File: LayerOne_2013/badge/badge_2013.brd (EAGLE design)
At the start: 81.3 x 81.3 mm, 81 parts, among them CON6 J8, CON8 J3, J6 con1, U1 UG-2864HSWEG01, U3 TL064D

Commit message: usb
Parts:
- removed U$1: USB-MINIB-5PIN, SparkFun:USB-MINIB
- added JP6: USB-RECEPTABLE, daspilker:FCI-10103594-0001LF
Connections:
- net D+: now also JP6.3; no longer U$1.D+
- net D-: now also JP6.2; no longer U$1.D-
- net GND: now also JP6.5; no longer U$1.GND
- net VBUS: now also JP6.1; no longer U$1.VBUS
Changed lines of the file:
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@@
 <setting verticaltext="up"/>
 </settings>
-<grid distance="0.05" unitdist="inch" unit="inch" style="lines" multiple="1" display="yes" altdistance="0.005" altunitdist="inch" altunit="inch"/>
+<grid distance="0.05" unitdist="inch" unit="inch" style="lines" multiple="1" display="no" altdistance="0.005" altunitdist="inch" altunit="inch"/>
 <layers>
 <layer number="1" name="Top" color="4" fill="1" visible="yes" active="yes"/>
@@
 <element name="LED48" library="led" package="LED3MM" value="" x="4.97331875" y="37.77488125" rot="R172.5"/>
 <element name="U3" library="linear" package="SO14" value="TL064D" x="27.94" y="10.16"/>
-<element name="U$1" library="SparkFun" package="USB-MINIB" value="USB-MINIB-5PIN" x="-27.94" y="1.27" rot="MR180"/>
 <element name="BAT1" library="tvbgone-adj" package="BATTERY_CR123A" value="CR123A" x="0" y="0" rot="MR180"/>
 <element name="U1" library="microbuilder" package="UG-2864HSWEG01_0.96IN_WRAPAROUND" value="UG-2864HSWEG01" x="0" y="25.4" rot="MR180"/>
@@
 <element name="D3" library="microbuilder" package="CHIPLED_0805" value="" x="-17.78" y="-3.81"/>
 <element name="C12" library="SparkFun" package="0805" value="0.1uF" x="26.67" y="-17.78"/>
+<element name="JP6" library="daspilker" package="FCI-10103594-0001LF" value="USB-RECEPTABLE" x="-35.56" y="-46.99"/>
 </elements>
 <signals>
@@
 <contactref element="C21" pad="1"/>
 <contactref element="C19" pad="1"/>
-<contactref element="U$1" pad="GND"/>
 <contactref element="U1" pad="1"/>
 <contactref element="CON6" pad="1"/>
@@
 <contactref element="IC3" pad="1"/>
 <contactref element="BAT1" pad="-"/>
-<wire x1="26.4" y1="0.75" x2="22.86" y2="13.97" width="0" layer="19" extent="16-16"/>
-<wire x1="28.31" y1="-2.54" x2="26.4" y2="0.75" width="0" layer="19" extent="1-16"/>
+<contactref element="JP6" pad="5"/>
+<wire x1="-17.78" y1="-2.76" x2="-34.26" y2="-42.465" width="0" layer="19" extent="1-1"/>
+<wire x1="-19" y1="0" x2="-17.78" y2="-2.76" width="0" layer="19" extent="1-1"/>
+<wire x1="-12.7" y1="-2.76" x2="-17.78" y2="-2.76" width="0" layer="19" extent="1-1"/>
+<wire x1="-23.065" y1="3.95" x2="-19" y2="0" width="0" layer="19" extent="1-1"/>
+<wire x1="-5.75" y1="-1.6" x2="-12.7" y2="-2.76" width="0" layer="19" extent="1-1"/>
+<wire x1="0.8" y1="-5.75" x2="-5.75" y2="-1.6" width="0" layer="19" extent="1-1"/>
+<wire x1="5.75" y1="1.6" x2="0.8" y2="-5.75" width="0" layer="19" extent="1-1"/>
+<wire x1="0.8" y1="5.75" x2="5.75" y2="1.6" width="0" layer="19" extent="1-1"/>
+<wire x1="23.065" y1="-3.95" x2="5.75" y2="1.6" width="0" layer="19" extent="1-1"/>
+<wire x1="24.5" y1="-2.54" x2="23.065" y2="-3.95" width="0" layer="19" extent="1-1"/>
+<wire x1="28.31" y1="-2.54" x2="24.5" y2="-2.54" width="0" layer="19" extent="1-1"/>
 <wire x1="32.12" y1="-2.54" x2="28.31" y2="-2.54" width="0" layer="19" extent="1-1"/>
-<wire x1="24.5" y1="-2.54" x2="26.4" y2="0.75" width="0" layer="19" extent="1-16"/>
-<wire x1="23.065" y1="-3.95" x2="24.5" y2="-2.54" width="0" layer="19" extent="1-1"/>
+<wire x1="26.4" y1="0.75" x2="24.5" y2="-2.54" width="0" layer="19" extent="1-16"/>
 <wire x1="25.72" y1="-10.16" x2="23.065" y2="-3.95" width="0" layer="19" extent="1-1"/>
 <wire x1="30.8" y1="-10.16" x2="25.72" y2="-10.16" width="0" layer="19" extent="1-1"/>
 <wire x1="27.57" y1="-17.78" x2="25.72" y2="-10.16" width="0" layer="19" extent="1-1"/>
-<wire x1="5.75" y1="1.6" x2="23.065" y2="-3.95" width="0" layer="19" extent="1-1"/>
-<wire x1="0.8" y1="5.75" x2="5.75" y2="1.6" width="0" layer="19" extent="1-1"/>
-<wire x1="0.8" y1="-5.75" x2="5.75" y2="1.6" width="0" layer="19" extent="1-1"/>
-<wire x1="-5.75" y1="-1.6" x2="0.8" y2="-5.75" width="0" layer="19" extent="1-1"/>
-<wire x1="-12.7" y1="-2.76" x2="-5.75" y2="-1.6" width="0" layer="19" extent="1-1"/>
-<wire x1="-17.78" y1="-2.76" x2="-12.7" y2="-2.76" width="0" layer="19" extent="1-1"/>
-<wire x1="-19" y1="0" x2="-17.78" y2="-2.76" width="0" layer="19" extent="1-1"/>
-<wire x1="-23.065" y1="3.95" x2="-19" y2="0" width="0" layer="19" extent="1-1"/>
-<wire x1="-25.44" y1="2.87" x2="-23.065" y2="3.95" width="0" layer="19" extent="1-16"/>
-<wire x1="-10.15" y1="26.6" x2="0.8" y2="5.75" width="0" layer="19" extent="1-16"/>
+<wire x1="22.86" y1="13.97" x2="26.4" y2="0.75" width="0" layer="19" extent="16-16"/>
+<wire x1="-10.15" y1="26.6" x2="0.8" y2="5.75" width="0" layer="19" extent="1-1"/>
 </signal>
 <signal name="N$2">
@@
 </signal>
 <signal name="VBUS">
-<contactref element="U$1" pad="VBUS"/>
 <contactref element="D1" pad="4"/>
-<wire x1="24.4" y1="0.95" x2="-25.44" y2="-0.33" width="0" layer="19" extent="16-16"/>
+<contactref element="JP6" pad="1"/>
+<wire x1="24.4" y1="0.95" x2="-36.86" y2="-42.465" width="0" layer="19" extent="1-16"/>
 </signal>
 <signal name="D-">
 <contactref element="D1" pad="2"/>
-<contactref element="U$1" pad="D-"/>
-<wire x1="-25.44" y1="0.47" x2="26.4" y2="-0.95" width="0" layer="19" extent="16-16"/>
+<contactref element="JP6" pad="2"/>
+<wire x1="26.4" y1="-0.95" x2="-36.21" y2="-42.465" width="0" layer="19" extent="1-16"/>
 </signal>
 <signal name="D+">
 <contactref element="D1" pad="3"/>
-<contactref element="U$1" pad="D+"/>
-<wire x1="24.4" y1="-0.95" x2="-25.44" y2="1.27" width="0" layer="19" extent="16-16"/>
+<contactref element="JP6" pad="3"/>
+<wire x1="24.4" y1="-0.95" x2="-35.56" y2="-42.465" width="0" layer="19" extent="1-16"/>
 </signal>
 <signal name="N$21">

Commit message: 
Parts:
- renumbered R1 to R1T, R2 to R2T
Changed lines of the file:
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@@
 <element name="IC2" library="Outline" package="NONOLITH_TQFP-44" value="" x="0" y="0"/>
 <element name="IC1" library="23b_clock_noleds" package="HTSSOP32DAP" value="" x="-27.94" y="0" rot="R180"/>
-<element name="R1" library="rcl" package="R0805" value="20K" x="31.75" y="-10.16"/>
+<element name="R1T" library="rcl" package="R0805" value="20K" x="31.75" y="-10.16"/>
 <element name="IC3" library="23b_clock_noleds" package="HTSSOP32DAP" value="" x="27.94" y="0"/>
-<element name="R2" library="rcl" package="R0805" value="20K" x="26.67" y="-10.16"/>
+<element name="R2T" library="rcl" package="R0805" value="20K" x="26.67" y="-10.16"/>
 <element name="LED1" library="led" package="LED3MM" value="" x="0" y="38.1" rot="R180"/>
 <element name="LED2" library="led" package="LED3MM" value="" x="-4.97331875" y="37.77488125" rot="R187.5"/>
@@
 <contactref element="D3" pad="C"/>
 <contactref element="C12" pad="2"/>
-<contactref element="R1" pad="1"/>
+<contactref element="R1T" pad="1"/>
 <contactref element="IC1" pad="1"/>
-<contactref element="R2" pad="1"/>
+<contactref element="R2T" pad="1"/>
 <contactref element="IC3" pad="1"/>
 <contactref element="BAT1" pad="-"/>
@@
 <signal name="N$13">
 <contactref element="IC1" pad="31"/>
-<contactref element="R1" pad="2"/>
+<contactref element="R1T" pad="2"/>
 <wire x1="32.7" y1="-10.16" x2="-23.715" y2="-3.95" width="0" layer="19" extent="1-1"/>
 </signal>
@@
 <signal name="N$1">
 <contactref element="IC3" pad="31"/>
-<contactref element="R2" pad="2"/>
+<contactref element="R2T" pad="2"/>
 <wire x1="27.62" y1="-10.16" x2="23.715" y2="3.95" width="0" layer="19" extent="1-1"/>
 </signal>

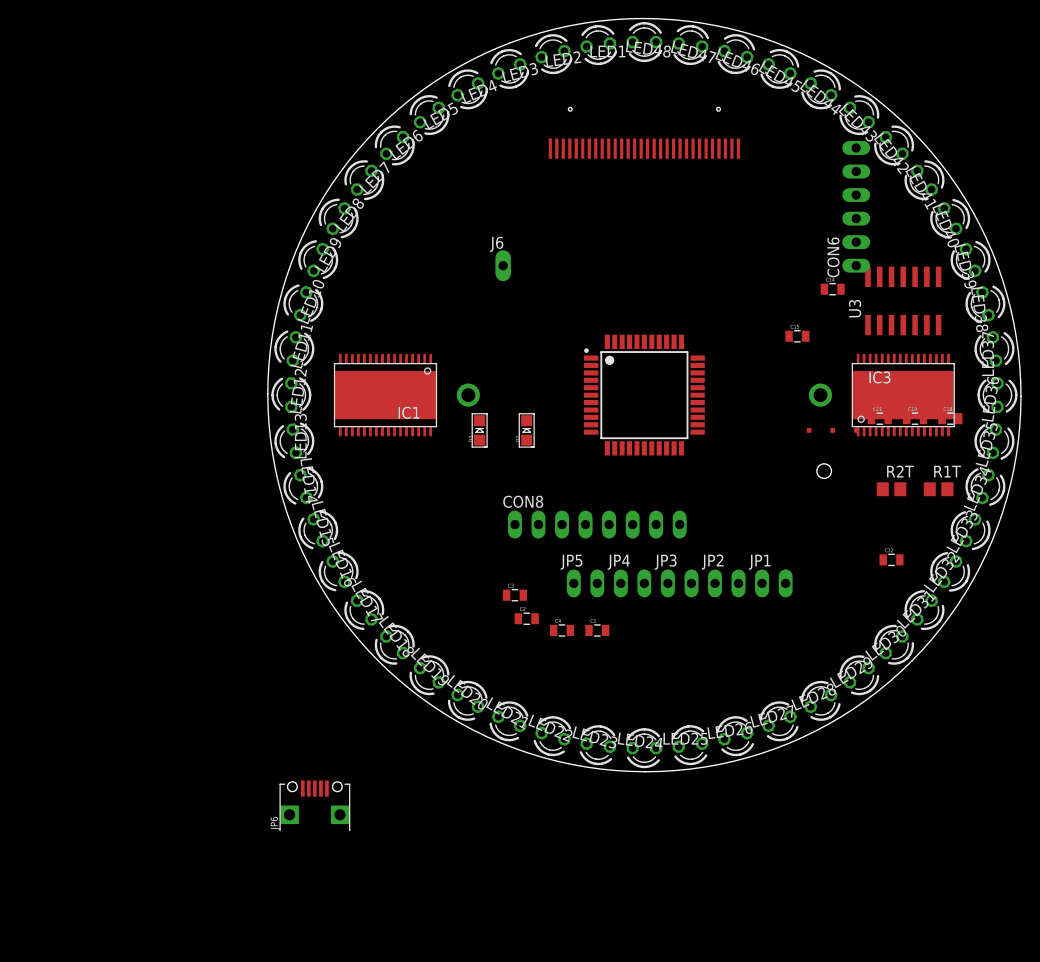
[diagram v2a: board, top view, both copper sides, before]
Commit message: 
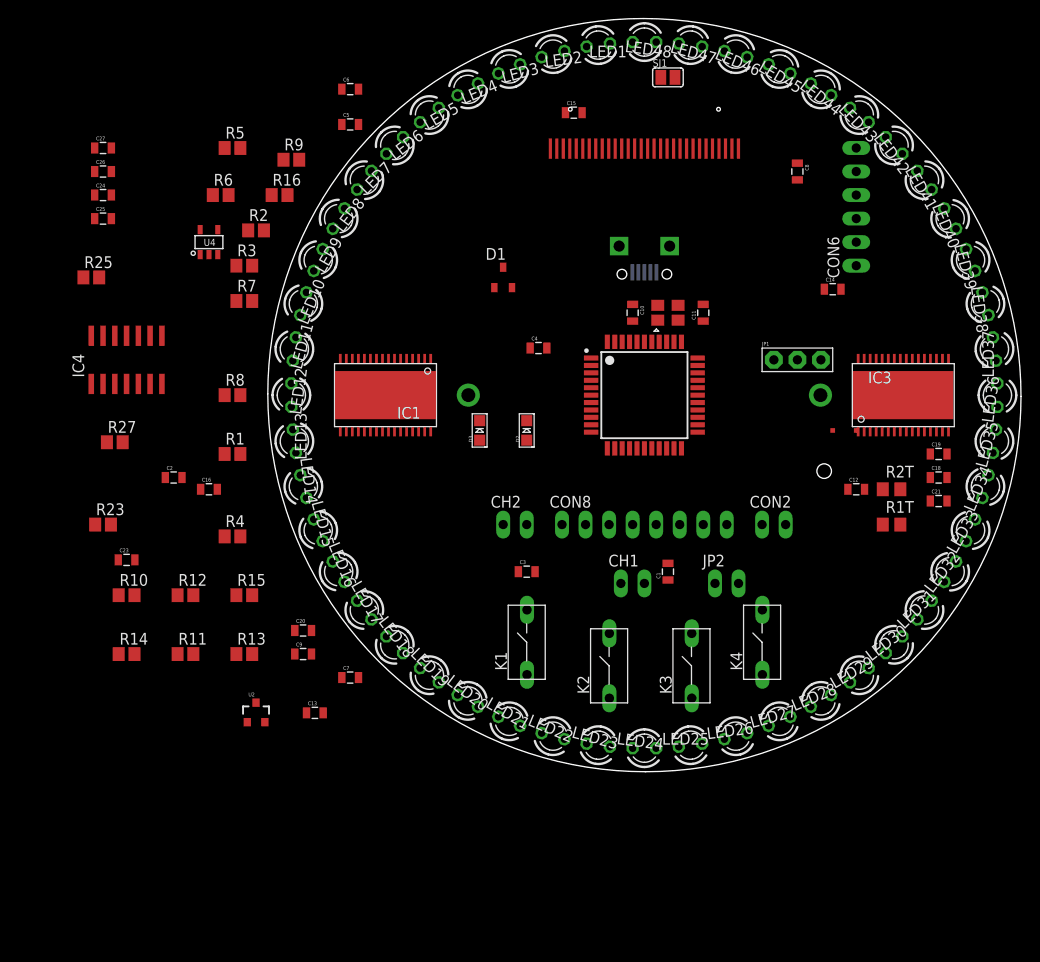
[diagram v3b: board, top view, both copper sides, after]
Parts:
- removed J6: con1, microbuilder:1X01_OVAL
- removed JP3, JP5: (no value), microbuilder:1X02_OVAL
- removed TP3: TEST-POINT2, SparkFun:PAD.02X.02
- removed U3: TL064D, linear:SO14
- added C10, C11, C24, C26, C5, C6, C7: 0.1uF, SparkFun:0805
- added C13, C20, C27, C8: 4.7uF, SparkFun:0805
- added C16, C9: 330pF, SparkFun:0805
- added C23: 10pF, SparkFun:0805
- added C25: 1uF, SparkFun:0805
- added CH2: CON2, microbuilder:1X02_OVAL
- added CON2: EXT, microbuilder:1X02_OVAL
- added IC4: TL064D, linear:SO14
- added K1, K2, K3, K4: (no value), switch-omron:B3F-5XX
- added R1, R11, R13, R4, R5, R6: 3K, resistor:R0805
- added R10, R2: 820K, resistor:R0805
- added R12, R27, R3: 180K, resistor:R0805
- added R14, R7: 20K, resistor:R0805
- added R15, R8: 180k, resistor:R0805
- added R16: 820k, resistor:R0805
- added R23, R25: 360K, resistor:R0805
- added R9: 20.0K, resistor:R0805
- added SJ1: (no value), microbuilder:SOLDERJUMPER_REFLOW_NOPASTE
- added U2: AP7333-33SOT23-3, SparkFun:SOT23-3
- added U4: TPS60403, RHD2000_eval_board:SOT-23-5
- added X2: NX3225GA, M6-RF315:NX3225GA
- added Z1: PRTR5V0U2X, USBug:SOT143B
- C1: value 0.1uF -> 1uF
- C2: value 0.1uF -> 330pF
- CH1: value (none) -> CON2
- D1: value PRTR5V0U2X -> LM4040d20; device USBug:SOT143B -> texas:DBZ_R-PDSO-G3
- JP1: device microbuilder:1X02_OVAL -> microbuilder:JUMPER3
- TP1: value TEST-POINT2 -> TP-2.048V
- TP2: value TEST-POINT2 -> (none)
- moved JP6 73.9 mm to (0.00, 17.8), flipped to the bottom, turned to 180 degrees
- moved D1 42.6 mm to (-15.2, 12.7), flipped to the top, turned to 0 degrees
- moved C2 41.0 mm to (-50.8, -8.89)
- moved C15 34.1 mm to (-7.62, 30.5)
- moved C4 30.6 mm to (-11.4, 5.08)
- moved JP1 24.3 mm to (16.5, 3.81)
- moved C21 10.9 mm to (31.8, -11.4)
- moved C1 9.92 mm to (2.54, -19.1), turned to 90 degrees
- moved C12 8.52 mm to (22.9, -10.2)
- moved C18 6.48 mm to (31.8, -8.89)
- moved R1T 6.35 mm to (26.7, -14.0)
- moved CON8 5.08 mm to (0.00, -14.0)
- moved C19 4.58 mm to (31.8, -6.35)
- moved C3 2.84 mm to (-12.7, -19.1)
- renumbered JP4 to CH1
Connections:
- net N$6 renamed RX
- net N$7 renamed PWR
- net N$8 renamed TX
- net N$9 renamed LNK
- removed net V+: U3.4
- removed net V-: U3.11
- removed net VBAT: U1.6
- removed net VCC: BAT1.+, C18.2, C19.2, C21.2, IC1.32, IC2.19, IC2.31, IC2.9, IC3.32, LED1.A, LED10.A, LED11.A, LED12.A, LED13.A, LED14.A, LED15.A, LED16.A, LED17.A, LED18.A, LED19.A, LED2.A, LED20.A, LED21.A, LED22.A, LED23.A, LED24.A, LED25.A, LED26.A, LED27.A, LED28.A, LED29.A, LED3.A, LED30.A, LED31.A, LED32.A, LED33.A, LED34.A, LED35.A, LED36.A, LED37.A, LED38.A, LED39.A, LED4.A, LED40.A, LED41.A, LED42.A, LED43.A, LED44.A, LED45.A, LED46.A, LED47.A, LED48.A, LED5.A, LED6.A, LED7.A, LED8.A, LED9.A, U1.28
- removed net VDD: U1.9
- removed net VLSS: U1.29
- removed net VSS: U1.8
- new net !CS: IC2.4, U1.13
- new net !RES: IC2.5, U1.14
- new net +2.048V: C5.1, IC2.40, IC4.8, IC4.9, R13.1, R25.1, R4.1, R6.1, TP1.P$1
- new net +3.3V: C18.2, C19.2, C20.1, C21.2, IC1.32, IC2.19, IC2.31, IC2.9, IC3.32, JP1.2, LED1.A, LED10.A, LED11.A, LED12.A, LED13.A, LED14.A, LED15.A, LED16.A, LED17.A, LED18.A, LED19.A, LED2.A, LED20.A, LED21.A, LED22.A, LED23.A, LED24.A, LED25.A, LED26.A, LED27.A, LED28.A, LED29.A, LED3.A, LED30.A, LED31.A, LED32.A, LED33.A, LED34.A, LED35.A, LED36.A, LED37.A, LED38.A, LED39.A, LED4.A, LED40.A, LED41.A, LED42.A, LED43.A, LED44.A, LED45.A, LED46.A, LED47.A, LED48.A, LED5.A, LED6.A, LED7.A, LED8.A, LED9.A, U1.6, U1.9
- new net +3V3_OUT: C1.2, JP1.1, U2.2
- new net -5V: C26.2, C27.2, C7.1, IC4.11, U4.1
- new net BATTERY3V: BAT1.+, JP1.3
- new net D/C: IC2.6, U1.15
- new net DB2: SJ1.2, U1.20
- new net DB3: U1.21
- new net DB4: U1.22
- new net DB5: U1.23
- new net DB6: U1.24
- new net DB7: U1.25
- new net DGND: X2.2, X2.4
- new net E: U1.17
- new net N$20: IC4.12, R25.2, R27.1
- new net N$23: C6.1, D1.1, IC4.10, R9.2
- new net N$24: C23.1, IC4.13, R23.2
- new net N$25: IC4.5, R2.2, R3.1
- new net N$26: CH1.1, R2.1
- new net N$27: IC4.3, R10.2, R12.1
- new net N$28: IC4.6, R7.1, R8.2
- new net N$29: IC4.7, R1.1, R7.2
- new net N$30: CH2.1, R10.1
- new net N$31: IC4.2, R14.1, R15.2
- new net N$32: R16.2, U1.26
- new net N$33: C8.1, U1.27
- new net N$34: C13.1, U1.28
- new net N$35: IC4.1, R11.1, R14.2
- new net N$36: C11.2, IC2.36, X2.3
- new net N$37: C10.2, IC2.37, X2.1
- new net N$7: C23.2, IC4.14, JP2.1, R23.1
- new net N$8: C25.2, U4.5
- new net N$9: C25.1, U4.3
- new net PA1: IC2.41, K4.2
- new net PA2: IC2.42, K3.2
- new net PA3: IC2.43, K2.2
- new net PA4: IC2.44, K1.2
- new net PA5: C4.2, IC2.1, R5.2, R6.2
- new net PA6: C2.1, IC2.2, R1.2, R4.2
- new net PA7: C9.1, IC2.3, R11.2, R13.2
- new net R/W: U1.16
- new net RESET: IC2.35
- new net SCLK/DB0: IC2.21, U1.18
- new net SDIN/DB1: IC2.23, SJ1.1, U1.19
- new net TP-TEST: IC2.22, TP2.P$1
- net +5V: now also C16.2, C24.2, C3.1, IC4.4, JP6.1, R9.1, U2.1, U4.2
- net D+: now also IC2.27, Z1.3; no longer D1.3
- net D-: now also IC2.26, Z1.2; no longer D1.2
- net GND: now also C1.1, C10.1, C11.1, C13.2, C16.1, C2.2, C20.2, C24.1, C26.1, C27.1, C3.2, C4.1, C5.2, C6.2, C7.2, C8.2, C9.2, CH1.2, CH2.2, CON2.2, D1.2, JP2.2, K1.1, K2.1, K3.1, K4.1, R12.2, R15.1, R16.1, R27.2, R3.2, R5.1, R8.1, U1.10, U1.11, U1.12, U1.29, U1.30, U1.8, U2.3, U4.4, Z1.1; no longer D1.1
- net N$19: now also CON2.1; no longer JP1.2
- net VBUS: now also Z1.4; no longer D1.4, JP6.1

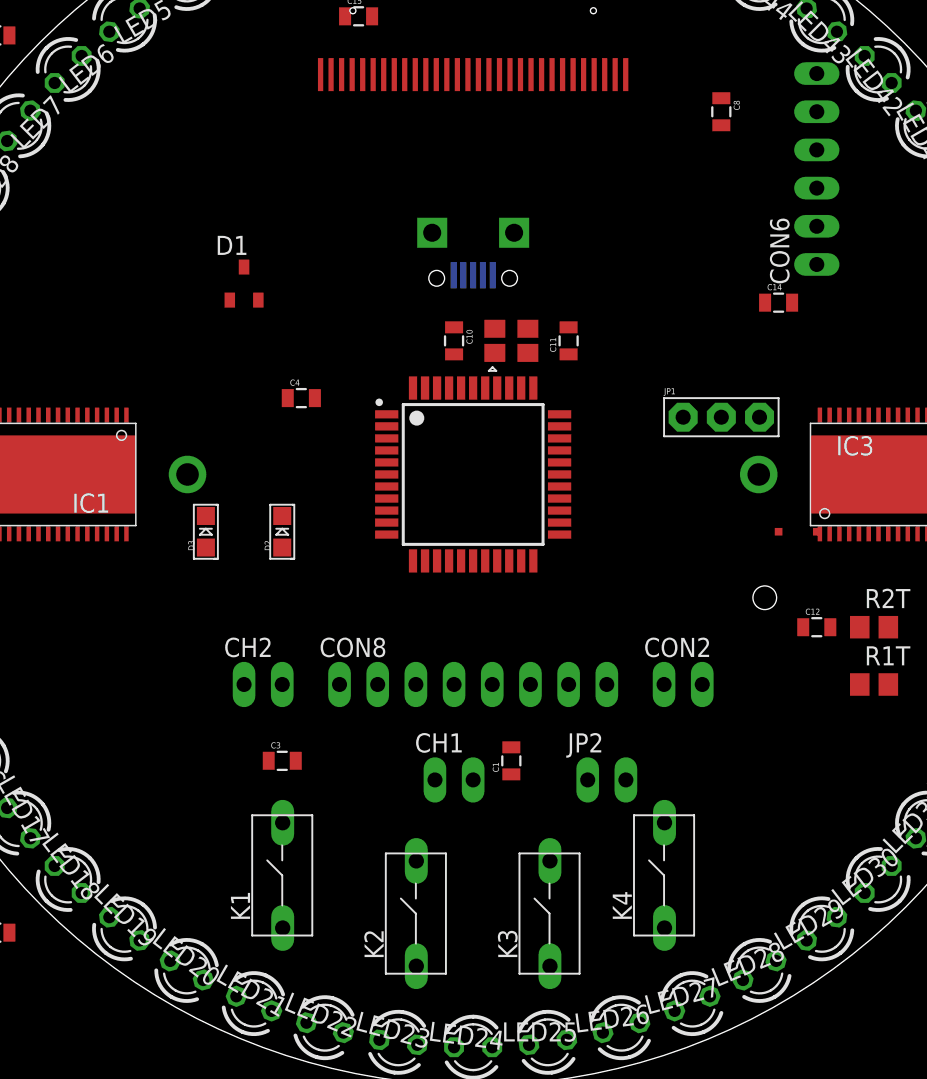
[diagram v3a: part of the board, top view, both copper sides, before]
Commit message: 
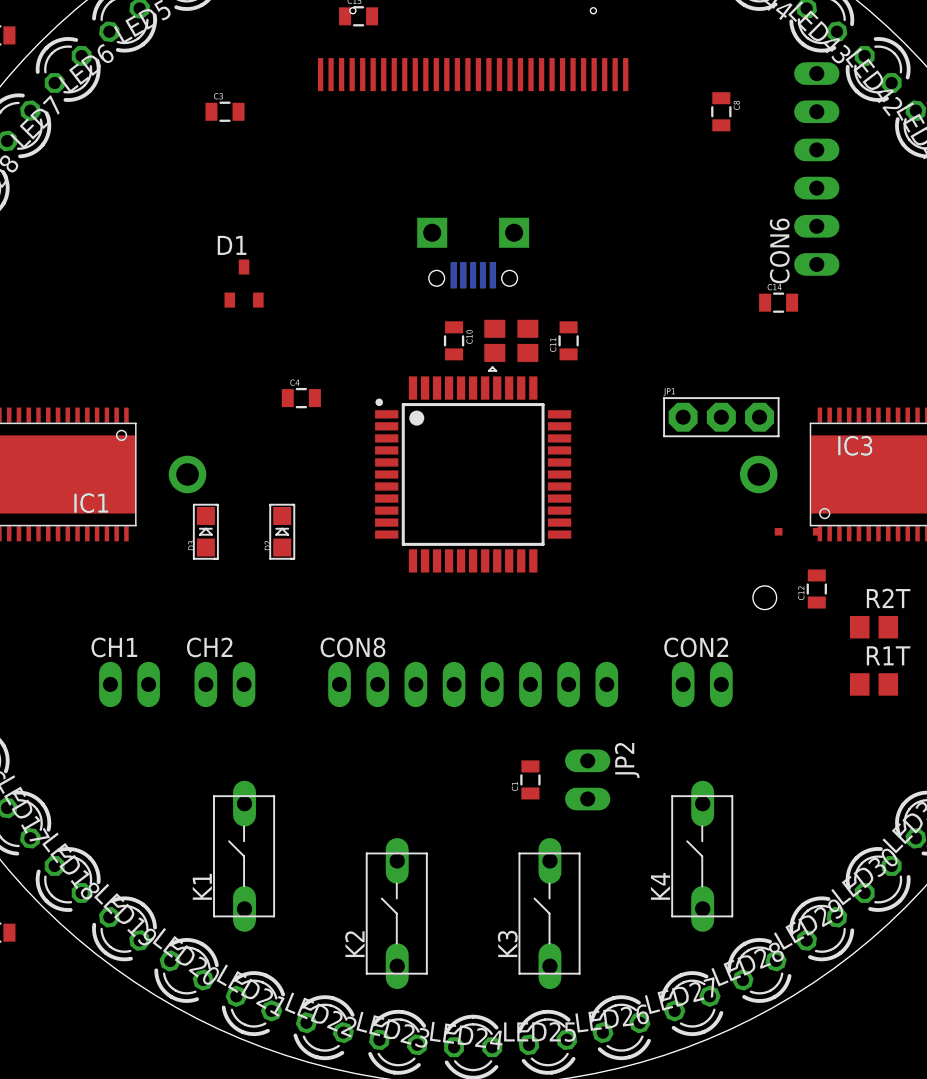
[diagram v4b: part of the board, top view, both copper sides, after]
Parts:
- C3, C6, C7: value 0.1uF -> 1uF
- D2: value (none) -> red
- D3: value (none) -> grn
- moved C3 43.3 mm to (-16.5, 24.1)
- moved CH1 22.5 mm to (-22.9, -14.0)
- moved K1 2.84 mm to (-15.2, -25.4)
- moved K4 2.84 mm to (15.2, -25.4)
- moved CH2 2.54 mm to (-16.5, -14.0)
- moved C12 2.54 mm to (22.9, -7.62), turned to 90 degrees
- moved C1 1.80 mm to (3.81, -20.3)
- moved JP2 1.27 mm to (7.62, -20.3), turned to 270 degrees
- moved K2 1.27 mm to (-5.08, -29.2)
- moved CON2 1.27 mm to (15.2, -14.0)
